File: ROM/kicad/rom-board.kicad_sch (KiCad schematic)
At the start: 11 parts

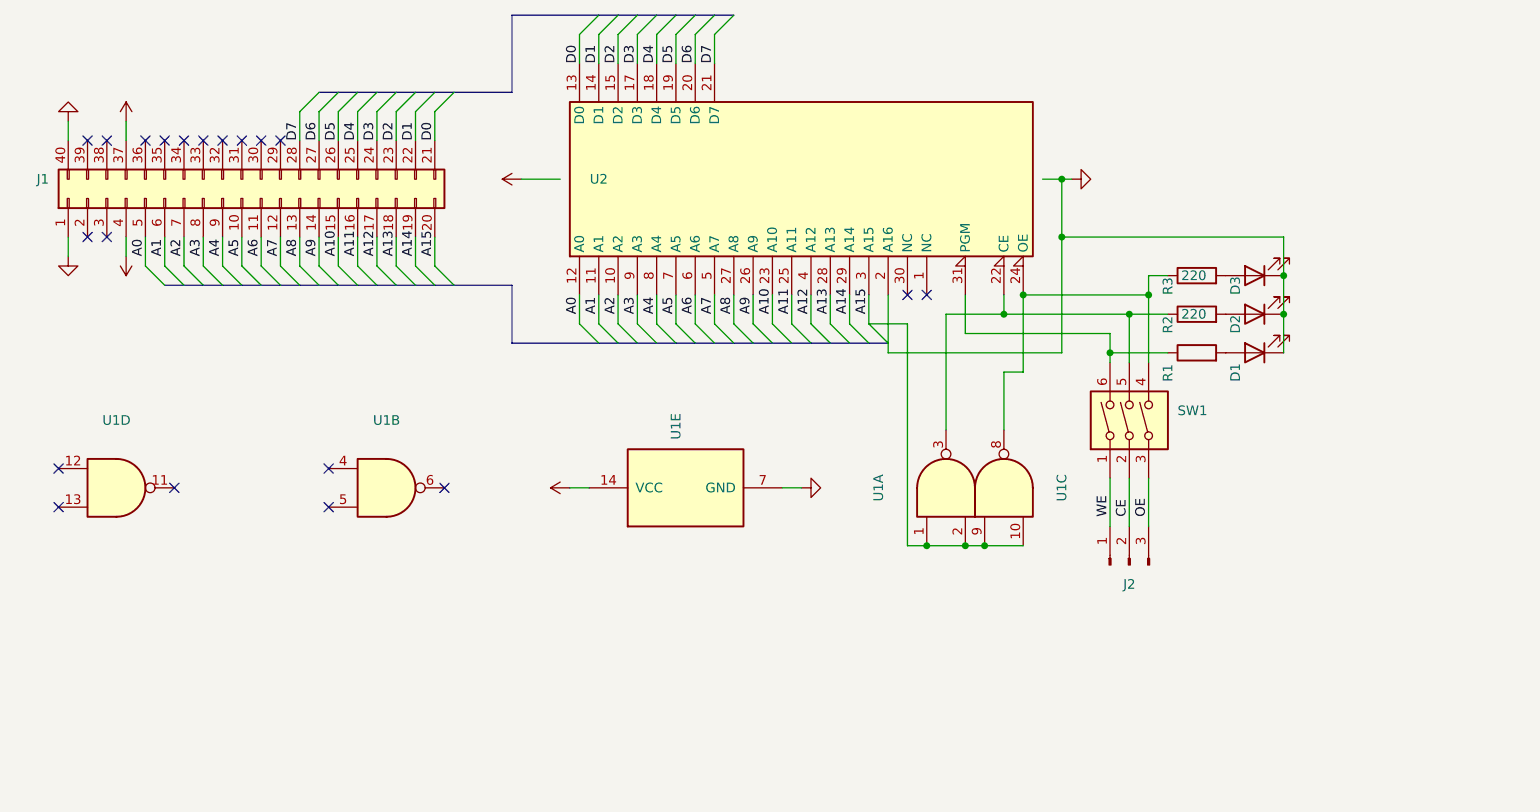
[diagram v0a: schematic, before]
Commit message: update ROM board; add log
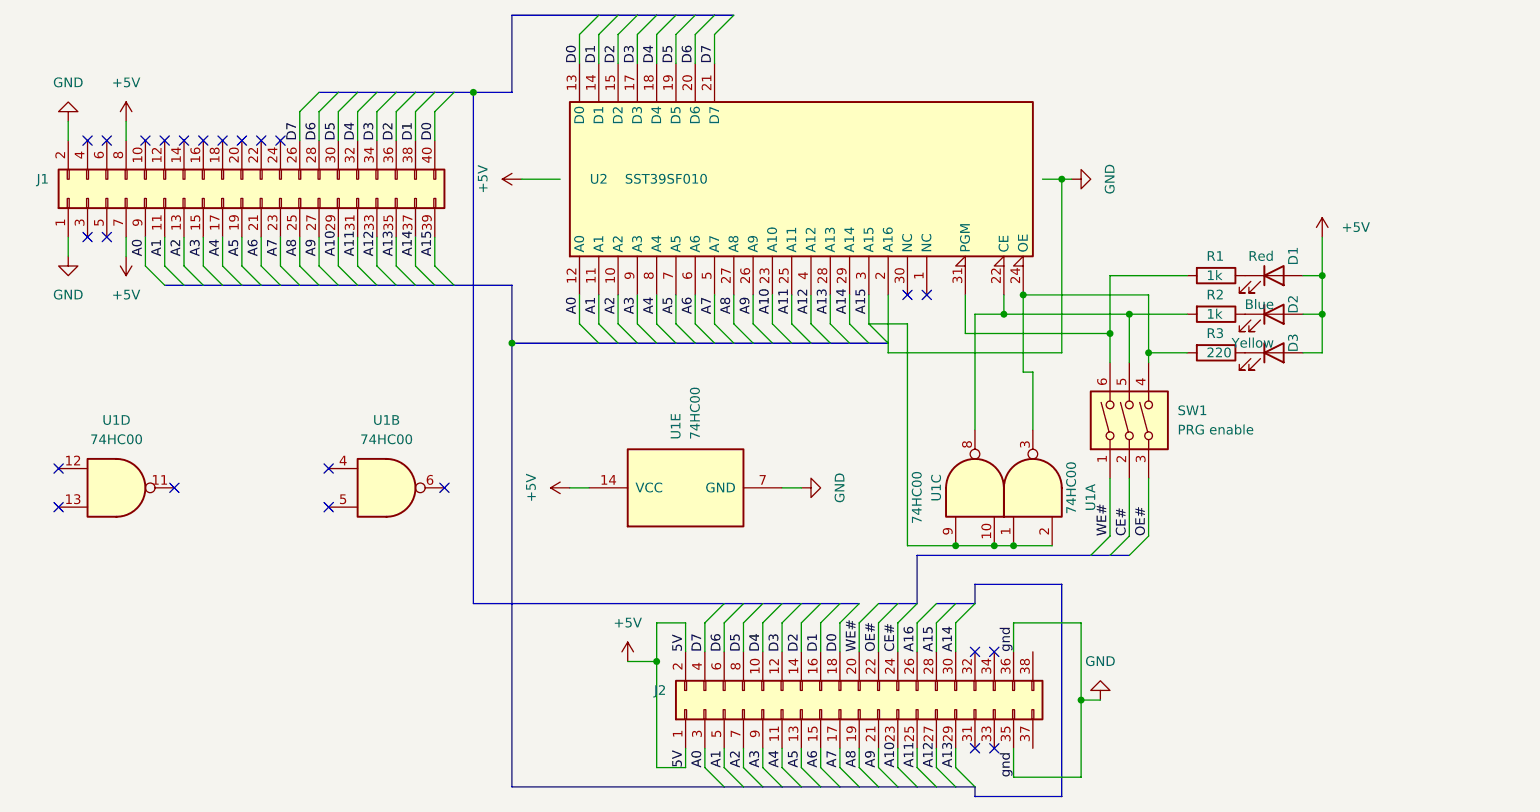
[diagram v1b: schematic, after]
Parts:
- removed J1: (no value), symbol Connector_Generic:Conn_02x20_Counter_Clockwise
- removed J2: (no value), symbol Connector:Conn_01x03_Male
- added J1: (no value), symbol Connector_Generic:Conn_02x20_Odd_Even
- added J2: (no value), symbol Connector_Generic:Conn_02x19_Odd_Even
- D1: value (none) -> Red; footprint (none) -> LED_THT:LED_D5.0mm
- D2: value (none) -> Blue; footprint (none) -> LED_THT:LED_D5.0mm
- D3: value (none) -> Yellow; footprint (none) -> LED_THT:LED_D5.0mm
- R1: value (none) -> 1k; footprint (none) -> Resistor_THT:R_Axial_DIN0204_L3.6mm_D1.6mm_P2.54mm_Vertical
- R2: value 220 -> 1k; footprint (none) -> Resistor_THT:R_Axial_DIN0204_L3.6mm_D1.6mm_P2.54mm_Vertical
- R3: footprint (none) -> Resistor_THT:R_Axial_DIN0204_L3.6mm_D1.6mm_P2.54mm_Vertical
- SW1: value (none) -> PRG enable; footprint (none) -> Package_DIP:DIP-6_W7.62mm
- U1: value (none) -> 74HC00; footprint (none) -> Package_DIP:DIP-14_W7.62mm
- U2: value (none) -> SST39SF010; footprint (none) -> Package_DIP:DIP-32_W15.24mm
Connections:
- net +5V: now also D1.2 (A), D2.2 (A), D3.2 (A), J1.7 (Pin_7), J1.8 (Pin_8), J2.1 (Pin_1), J2.2 (Pin_2)
- net A0: now also J1.9 (Pin_9), J2.3 (Pin_3)
- net A1: now also J1.11 (Pin_11), J2.5 (Pin_5)
- net A10: now also J1.29 (Pin_29), J2.23 (Pin_23)
- net A11: now also J1.31 (Pin_31), J2.25 (Pin_25)
- net A12: now also J1.33 (Pin_33), J2.27 (Pin_27)
- net A13: now also J1.35 (Pin_35), J2.29 (Pin_29)
- net A14: now also J1.37 (Pin_37), J2.30 (Pin_30)
- net A15: now also J1.39 (Pin_39), J2.28 (Pin_28)
- net A2: now also J1.13 (Pin_13), J2.7 (Pin_7)
- net A3: now also J1.15 (Pin_15), J2.9 (Pin_9)
- net A4: now also J1.17 (Pin_17), J2.11 (Pin_11)
- net A5: now also J1.19 (Pin_19), J2.13 (Pin_13)
- net A6: now also J1.21 (Pin_21), J2.15 (Pin_15)
- net A7: now also J1.23 (Pin_23), J2.17 (Pin_17)
- net A8: now also J1.25 (Pin_25), J2.19 (Pin_19)
- net A9: now also J1.27 (Pin_27), J2.21 (Pin_21)
- net D0: now also J1.40 (Pin_40), J2.18 (Pin_18)
- net D1: now also J1.38 (Pin_38), J2.16 (Pin_16)
- net D2: now also J1.36 (Pin_36), J2.14 (Pin_14)
- net D3: now also J1.34 (Pin_34), J2.12 (Pin_12)
- net D4: now also J1.32 (Pin_32), J2.10 (Pin_10)
- net D5: now also J1.30 (Pin_30), J2.8 (Pin_8)
- net D6: now also J1.28 (Pin_28), J2.6 (Pin_6)
- net D7: now also J1.26 (Pin_26), J2.4 (Pin_4)
- net GND: now also J1.1 (Pin_1), J1.2 (Pin_2), J2.35 (Pin_35), J2.36 (Pin_36); no longer D1.1 (K), D2.1 (K), D3.1 (K)
- net at SW1.5, U2.22 (CE): now also R2.2, U1.8; no longer R2.1, U1.3
- net at R1.2: now also SW1.6, U2.31 (PGM); no longer D1.2 (A)
- net at SW1.4, U2.24 (OE): now also R3.2, U1.3; no longer R3.1, U1.8
- net CE renamed CE#
- net CE#: now also J2.24 (Pin_24)
- net OE renamed OE#
- net OE#: now also J2.22 (Pin_22)
- net WE renamed WE#
- net WE#: now also J2.20 (Pin_20)
- new net: D2.1 (K), R2.1
- new net: D1.1 (K), R1.1
- new net: D3.1 (K), R3.1
- new net A16: J2.26 (Pin_26)
- no-connect marks 20 -> 24
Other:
- moved on the sheet: D1, D2, D3, R1, R2, R3, U1A, U1C

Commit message: fix build; fix 0xFF; add missing kicad
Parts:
- J1: value (none) -> BUS; footprint (none) -> Connector_PinSocket_2.54mm:PinSocket_2x20_P2.54mm_Vertical
- J2: value (none) -> Arduino; footprint (none) -> Connector_PinSocket_2.54mm:PinSocket_2x18_P2.54mm_Vertical
- SW1: value PRG enable -> Disconnect
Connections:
- net CE#: now also R2.2, SW1.1, U2.22 (CE); no longer SW1.2
- net OE#: now also R3.2, SW1.2, U2.24 (OE); no longer SW1.3
- net WE#: now also R1.2, U2.31 (PGM); no longer SW1.1
- net at SW1.5, U1.8: no longer R2.2, U2.22 (CE)
- new net: SW1.6, U1.3
- now unconnected: SW1.4
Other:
- moved on the sheet: D1, D2, D3, R1, R2, R3, SW1, U1A, U1B, U1C, U1E
